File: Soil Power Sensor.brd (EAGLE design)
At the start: 94 x 67 mm, 92 parts, among them IC1 TPD2E2U06DCK, J1 12401832E402A, U1 MAX9943ATT+, U10 FT234XD, U11 ESP32-C3-MINI-1-N4, U2 INA296A5, U3 THS4532, U4 FSA2466, U5 MAX11201A, U6 REF2033, U7 TLV1117LV33, U8 LM27761DSG, U9 WIO E5, X1 Voltage, X2 Current, X3 GND, X4 SDI, X5 SMA-142-0701-801/806

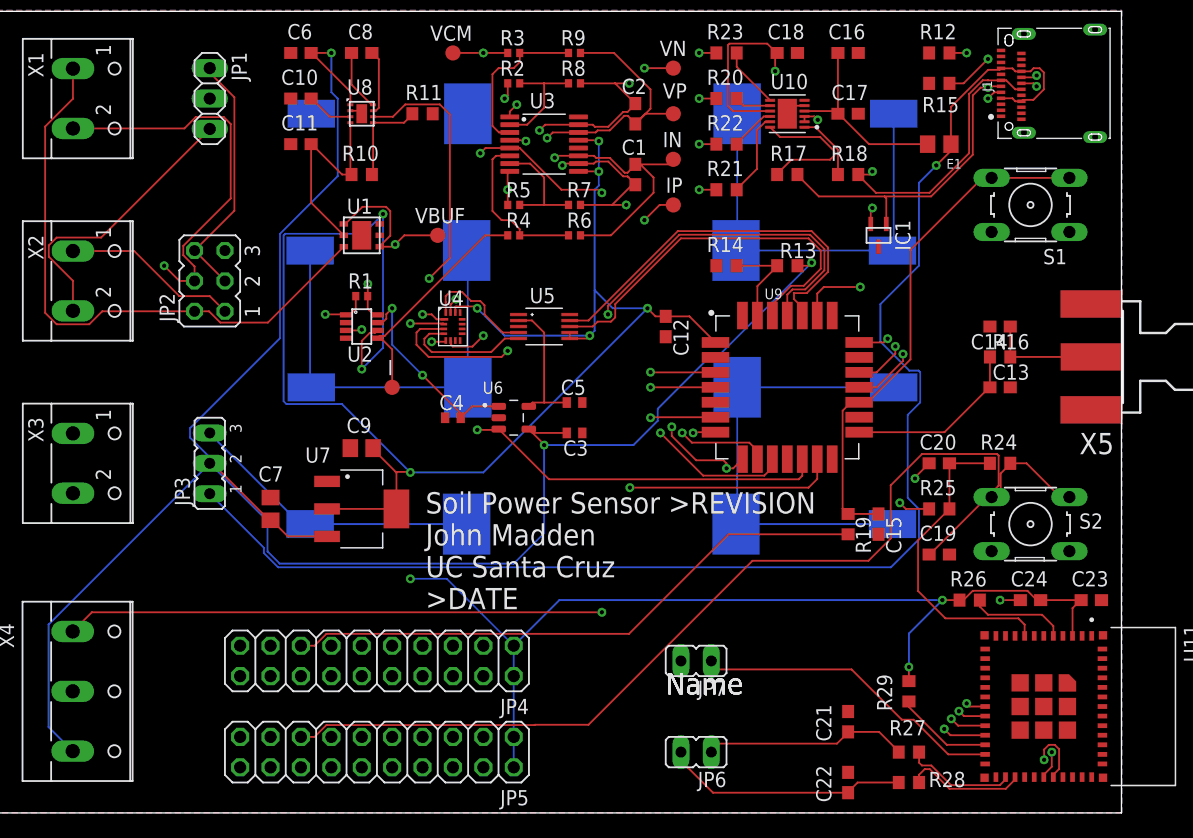
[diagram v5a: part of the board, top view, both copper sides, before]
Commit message: Added slug logo
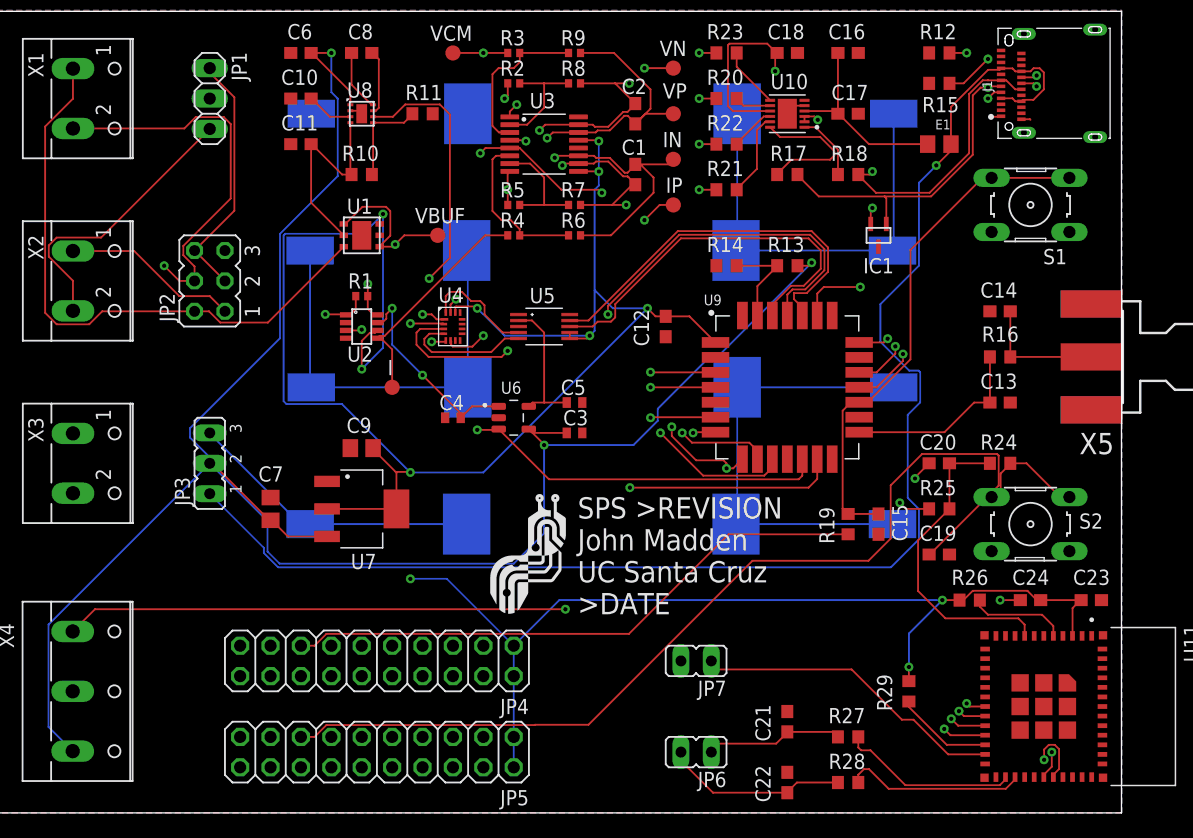
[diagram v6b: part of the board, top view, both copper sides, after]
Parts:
- moved R27 5.24 mm to (71.1, 6.35)
- moved C21 5.08 mm to (66.0, 7.62)
- moved C22 5.08 mm to (66.0, 2.54)
- moved R28 5.08 mm to (71.1, 2.54)
- moved C13 1.27 mm to (83.8, 34.3)
- moved C14 1.27 mm to (83.8, 41.9)
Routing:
- net D_N: track 9.28 -> 14.9 mm
- net N$39: track 17.5 -> 11.9 mm
- net N$40: track 20.4 -> 15.3 mm
- net D_P: track 10.1 -> 15.1 mm
- net N$22: track 86.7 -> 84.7 mm
- net GND: track 9.73 -> 11.4 mm
- net N$2: track 9.28 -> 10.6 mm
- net N$3: track 15.0 -> 15.8 mm
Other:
- board text added: "SPS >REVISION John Madden UC Santa Cruz >DATE"
- board text removed: "Name"
- board text removed: "Soil Power Sensor >REVISION John Madden UC Santa Cruz >DATE"

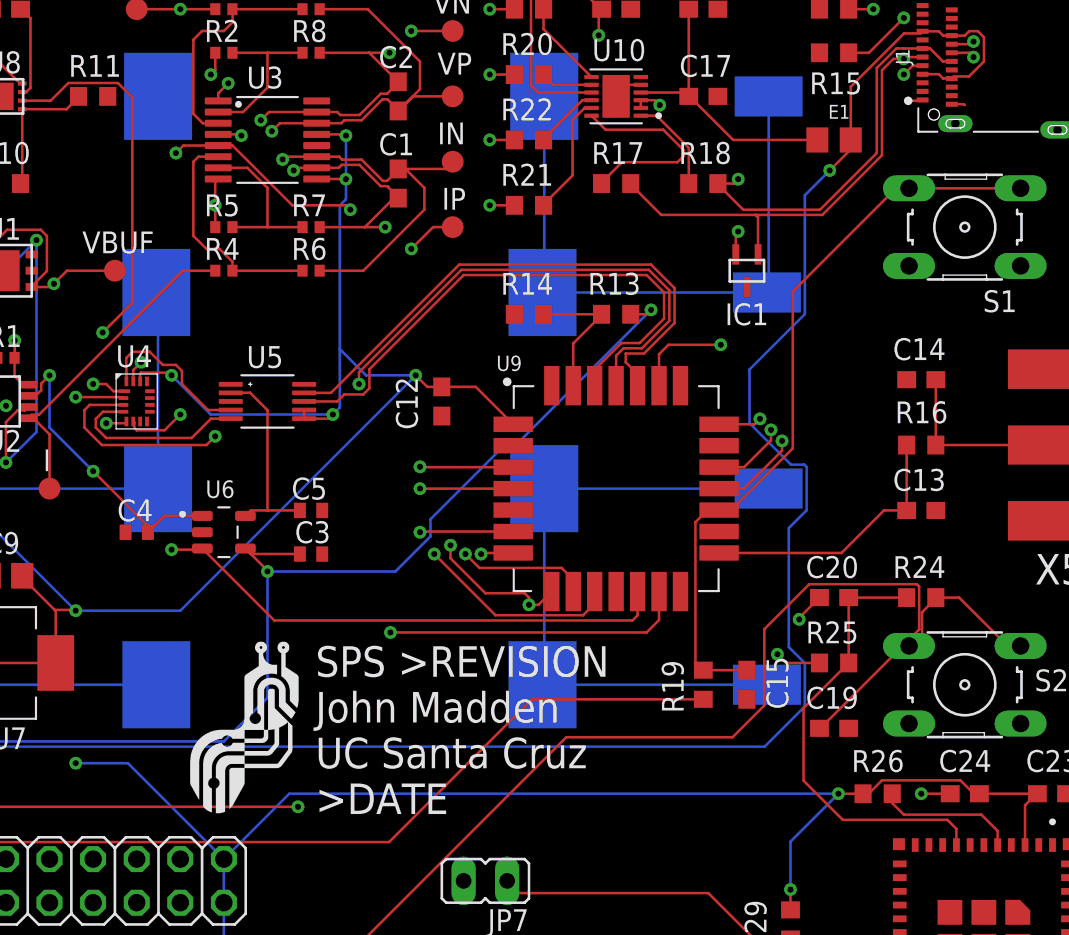
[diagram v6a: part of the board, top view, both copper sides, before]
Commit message: Fixed DRC errors
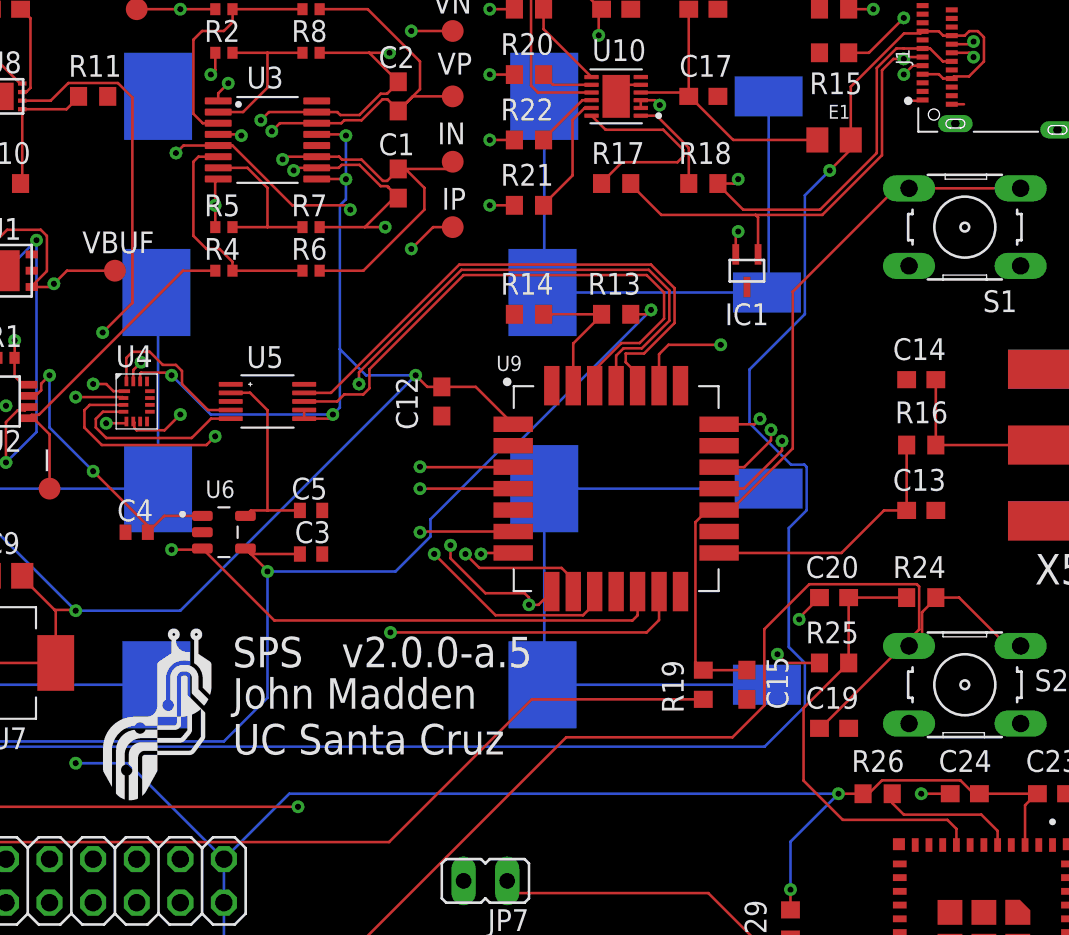
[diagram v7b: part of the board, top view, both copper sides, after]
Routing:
- net N$22: track 84.7 -> 86.2 mm
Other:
- board text added: ">LAST_DATE_TIME"
- board text added: ">REVISION"
- board text added: "John Madden UC Santa Cruz"
- board text added: "SPS"
- board text removed: "SPS >REVISION John Madden UC Santa Cruz >DATE"

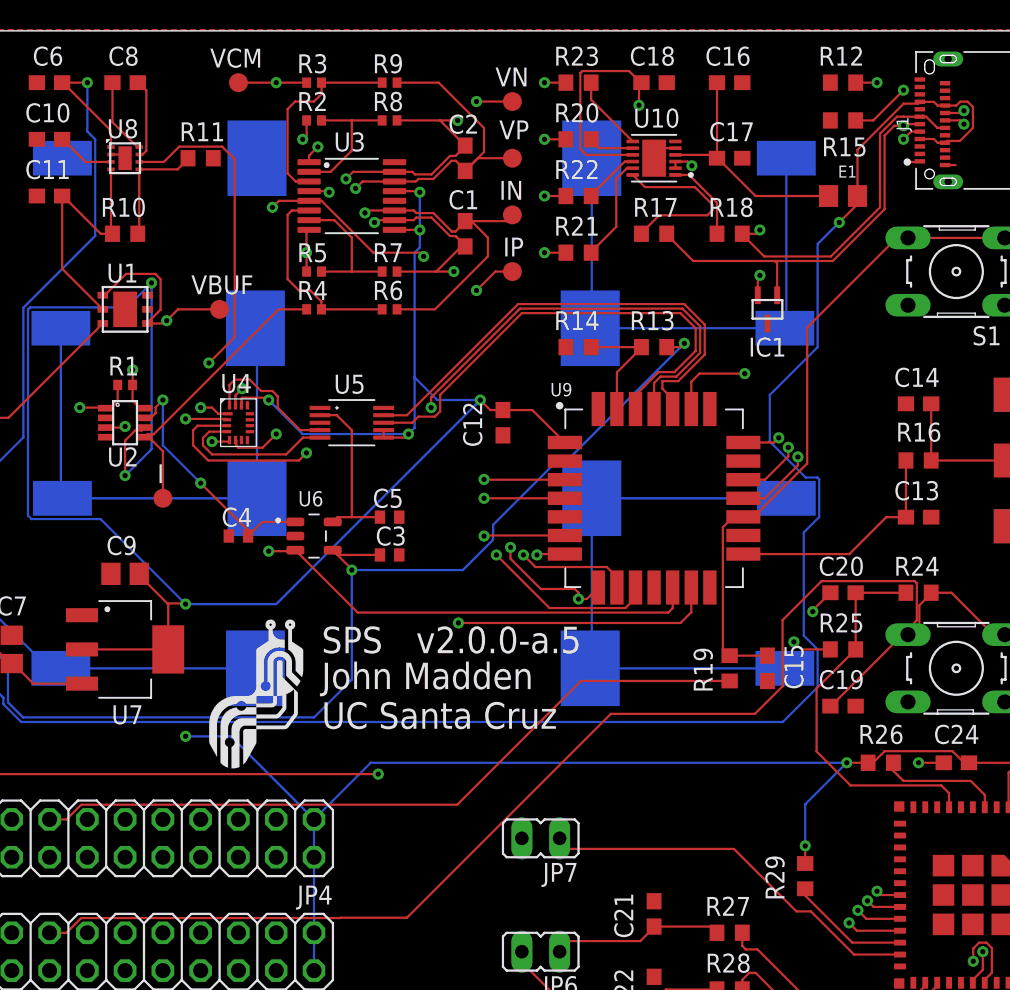
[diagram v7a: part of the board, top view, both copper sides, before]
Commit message: Replaced all 0402 components with 0603
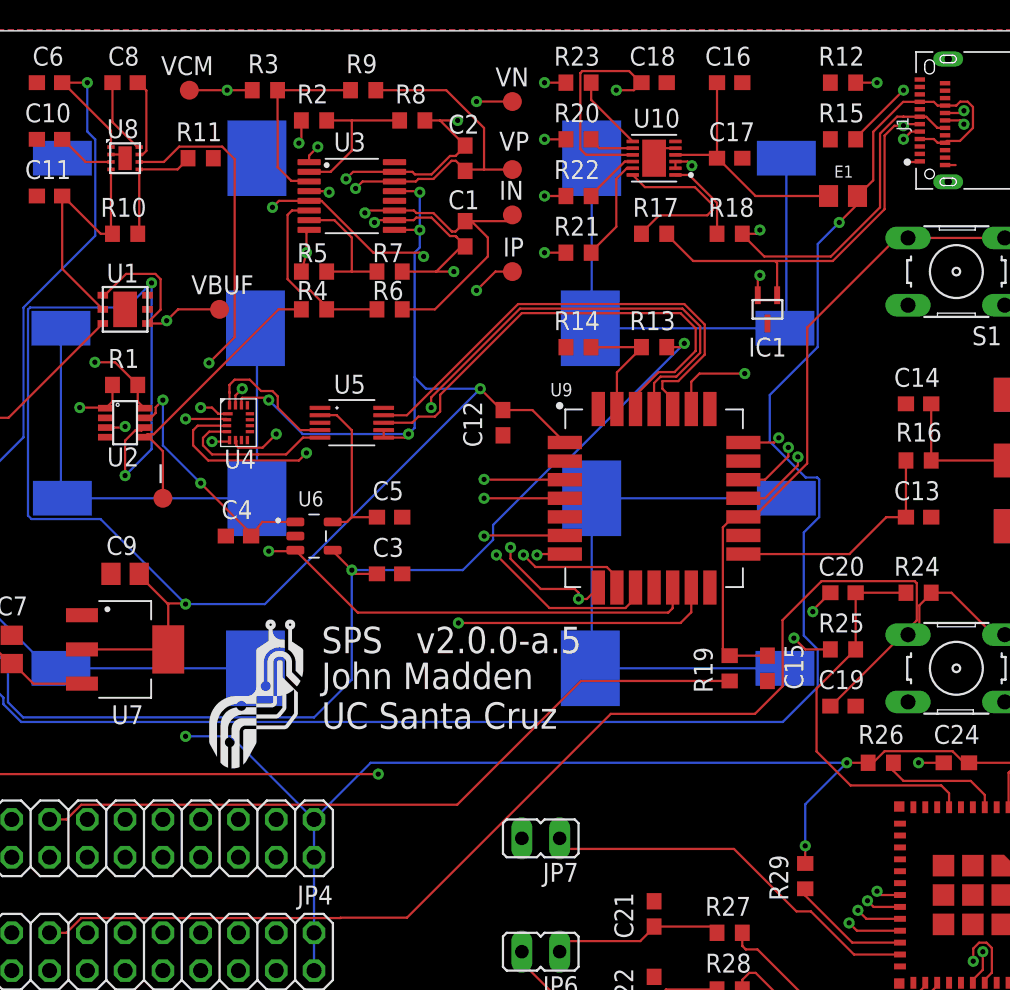
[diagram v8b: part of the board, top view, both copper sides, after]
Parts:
- C3, C4, C5: device rcl:C0402 -> rcl:C0603
- R1, R2, R3, R4, R5, R6, R7, R8, R9: device rcl:R0402 -> rcl:R0603
- moved R3 3.34 mm to (39.9, 63.0)
- moved VCM 3.34 mm to (34.8, 63.0)
- moved R9 1.85 mm to (46.5, 63.0)
- moved R8 1.52 mm to (49.8, 61.0)
- moved R15 1.27 mm to (78.7, 59.7)
- moved C3 1.27 mm to (48.3, 30.5)
- moved VP 0.76 mm to (56.5, 57.7)
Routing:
- net N$46: track 73.5 -> 71.2 mm
- net N$14: track 22.1 -> 24.0 mm
- net VOLTAGE_N: track 42.8 -> 41.0 mm
- net VCC: track 167.8 -> 166.3 mm
- net N$30: track 13.5 -> 12.6 mm
- net N$29: track 9.57 -> 10.4 mm
- net N$36: track 9.72 -> 9.02 mm
- net N$33: track 13.4 -> 12.8 mm
- net N$7: track 10.0 -> 10.6 mm
